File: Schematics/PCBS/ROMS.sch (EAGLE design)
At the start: 12 parts, among them IC1 ATMEGA328P-AU, M1 WIRELESS-NRF24L01-PA-EXT, Y1 16MHz

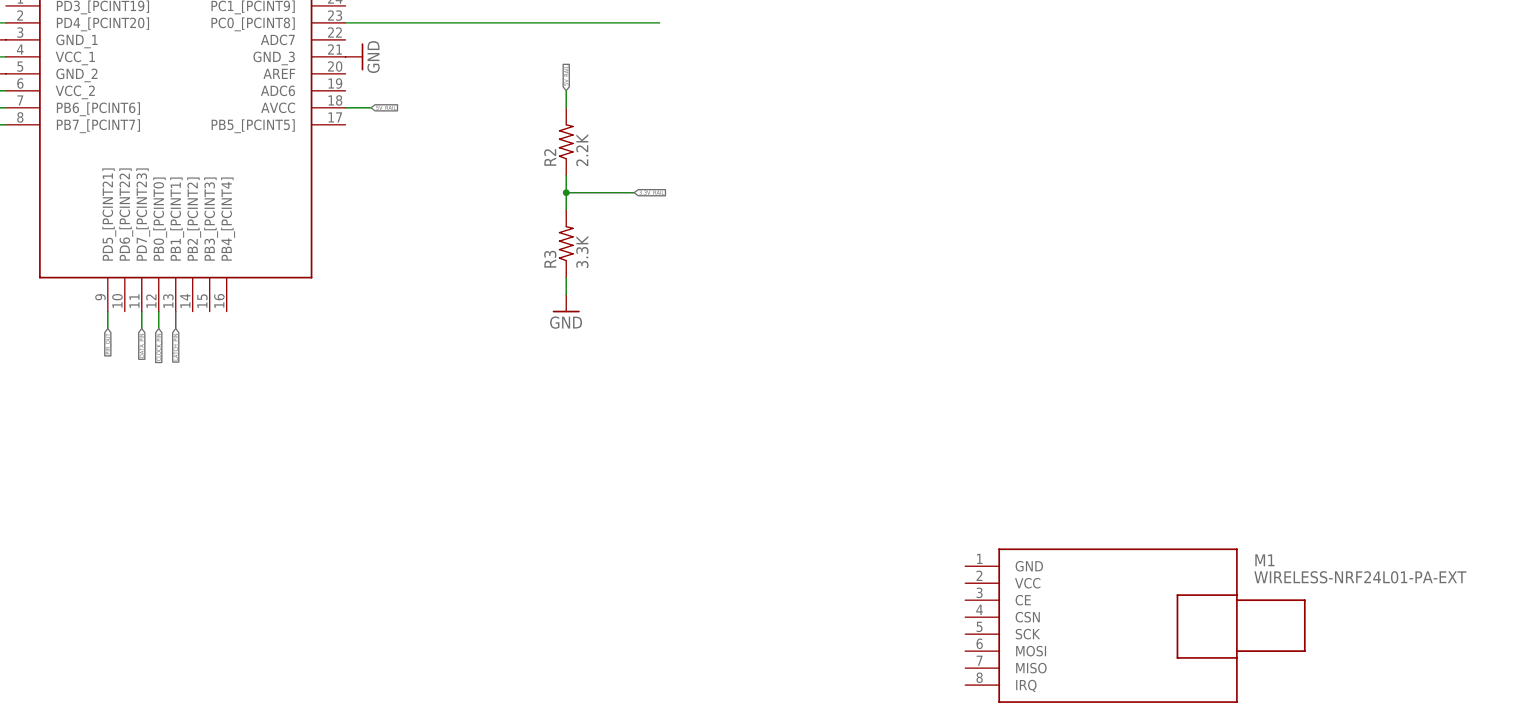
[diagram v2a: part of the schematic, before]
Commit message: connected NRF24 to ATMEGA328p
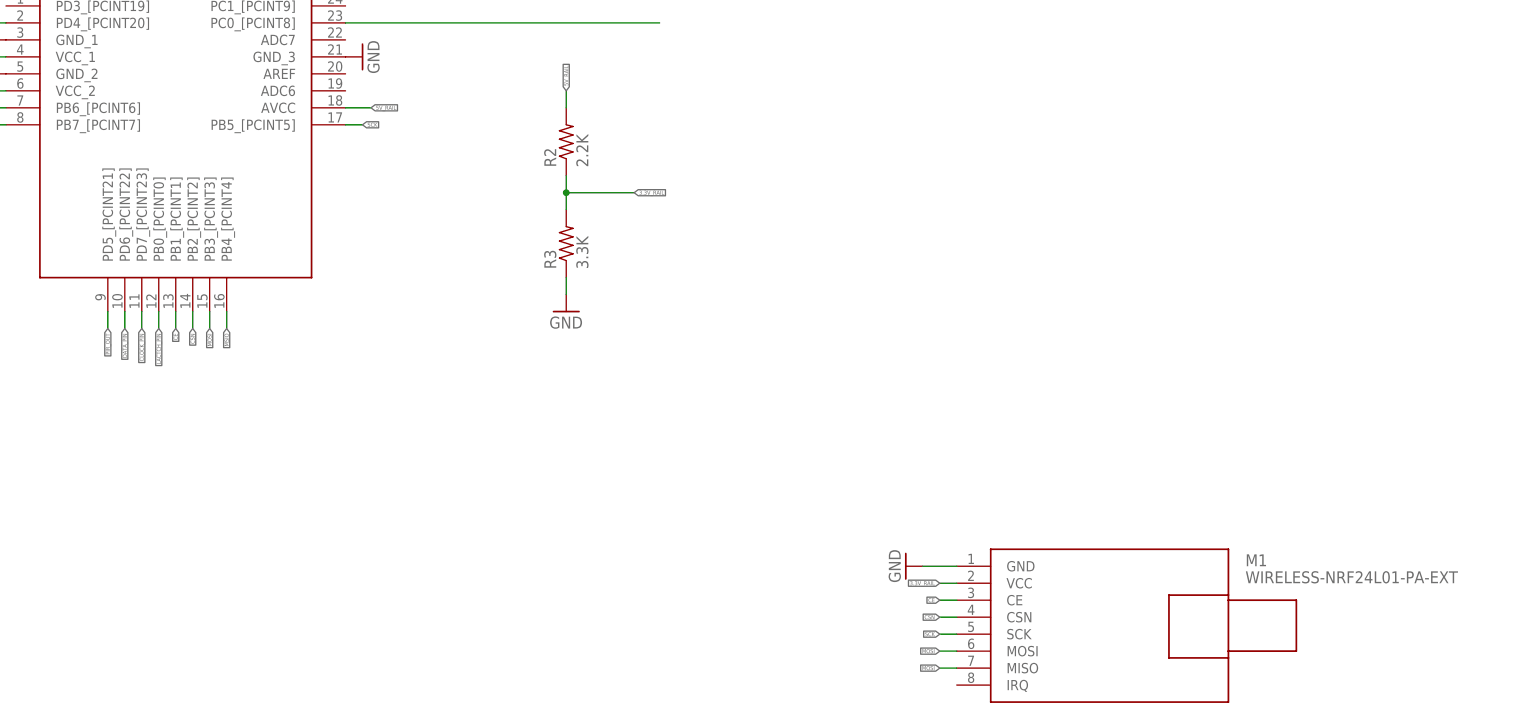
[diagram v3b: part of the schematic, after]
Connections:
- new net CE: IC1.PB1_[PCINT1], M1.CE
- new net CSN: IC1.PB2_[PCINT2], M1.CSN
- new net LACTCH_PIN: IC1.PB0_[PCINT0]
- new net MOSI: IC1.PB3_[PCINT3], M1.MISO, M1.MOSI
- new net MSIO: IC1.PB4_[PCINT4]
- new net SCK: IC1.PB5_[PCINT5], M1.SCK
- net 3.3V_RAIL: now also M1.VCC
- net CLOCK_PIN: now also IC1.PD7_[PCINT23]; no longer IC1.PB0_[PCINT0]
- net DATA_PIN: now also IC1.PD6_[PCINT22]; no longer IC1.PD7_[PCINT23]
- net GND: now also M1.GND
- net LATCH_PIN: no longer IC1.PB1_[PCINT1]
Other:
- moved on the sheet: M1
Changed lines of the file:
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@@
 <part name="R2" library="adafruit" library_urn="urn:adsk.eagle:library:420" deviceset="FLIPFLOP-RES" device="" package3d_urn="urn:adsk.eagle:package:6240726/1" value="2.2K"/>
 <part name="R3" library="adafruit" library_urn="urn:adsk.eagle:library:420" deviceset="FLIPFLOP-RES" device="" package3d_urn="urn:adsk.eagle:package:6240726/1" value="3.3K"/>
+<part name="GND11" library="supply1" library_urn="urn:adsk.eagle:library:371" deviceset="GND" device=""/>
 </parts>
 <sheets>
@@
 <attribute name="VALUE" x="69.85" y="101.6" size="1.778" layer="96" rot="R90"/>
 </instance>
-<instance part="M1" gate="G$1" x="217.17" y="-45.72" smashed="yes">
-<attribute name="NAME" x="237.49" y="-35.56" size="1.778" layer="95"/>
-<attribute name="VALUE" x="237.49" y="-38.1" size="1.778" layer="96"/>
+<instance part="M1" gate="G$1" x="215.9" y="-45.72" smashed="yes">
+<attribute name="NAME" x="236.22" y="-35.56" size="1.778" layer="95"/>
+<attribute name="VALUE" x="236.22" y="-38.1" size="1.778" layer="96"/>
 </instance>
 <instance part="GND7" gate="1" x="134.62" y="2.54" smashed="yes">
@@
 <attribute name="NAME" x="133.1214" y="8.89" size="1.778" layer="95" rot="R90"/>
 <attribute name="VALUE" x="137.922" y="8.89" size="1.778" layer="96" rot="R90"/>
+</instance>
+<instance part="GND11" gate="1" x="185.42" y="-35.56" smashed="yes" rot="R270">
+<attribute name="VALUE" x="182.88" y="-33.02" size="1.778" layer="96" rot="R270"/>
 </instance>
 </instances>
@@
 <pinref part="GND10" gate="1" pin="GND"/>
 </segment>
+<segment>
+<pinref part="M1" gate="G$1" pin="GND"/>
+<wire x1="193.04" y1="-35.56" x2="187.96" y2="-35.56" width="0.1524" layer="91"/>
+<pinref part="GND11" gate="1" pin="GND"/>
+</segment>
 </net>
 <net name="N$3" class="0">
@@
 <label x="-7.62" y="154.94" size="0.762" layer="95" xref="yes"/>
 </segment>
-<segment>
-<pinref part="IC1" gate="G$1" pin="PB1_[PCINT1]"/>
-<wire x1="76.2" y1="2.54" x2="76.2" y2="0" width="0.1524" layer="91"/>
-<label x="76.2" y="0" size="0.6096" layer="95" rot="R270" xref="yes"/>
-</segment>
 </net>
 <net name="CLOCK_PIN" class="0">
@@
 </segment>
 <segment>
-<pinref part="IC1" gate="G$1" pin="PB0_[PCINT0]"/>
-<wire x1="73.66" y1="2.54" x2="73.66" y2="0" width="0.1524" layer="91"/>
-<label x="73.66" y="0" size="0.6096" layer="95" rot="R270" xref="yes"/>
+<pinref part="IC1" gate="G$1" pin="PD7_[PCINT23]"/>
+<wire x1="71.12" y1="2.54" x2="71.12" y2="0" width="0.1524" layer="91"/>
+<label x="71.12" y="0" size="0.6096" layer="95" rot="R270" xref="yes"/>
 </segment>
 </net>
@@
 </segment>
 <segment>
-<pinref part="IC1" gate="G$1" pin="PD7_[PCINT23]"/>
-<wire x1="71.12" y1="2.54" x2="71.12" y2="0" width="0.1524" layer="91"/>
-<label x="71.12" y="0" size="0.6096" layer="95" rot="R270" xref="yes"/>
+<pinref part="IC1" gate="G$1" pin="PD6_[PCINT22]"/>
+<wire x1="68.58" y1="2.54" x2="68.58" y2="0" width="0.1524" layer="91"/>
+<label x="68.58" y="0" size="0.6096" layer="95" rot="R270" xref="yes"/>
 </segment>
 </net>
@@
 <junction x="134.62" y="20.32"/>
 </segment>
-</net>
+<segment>
+<pinref part="M1" gate="G$1" pin="VCC"/>
+<wire x1="193.04" y1="-38.1" x2="190.5" y2="-38.1" width="0.1524" layer="91"/>
+<label x="190.5" y="-38.1" size="0.6096" layer="95" rot="R180" xref="yes"/>
+</segment>
+</net>
+<net name="MOSI" class="0">
+<segment>
+<pinref part="IC1" gate="G$1" pin="PB3_[PCINT3]"/>
+<wire x1="81.28" y1="2.54" x2="81.28" y2="0" width="0.1524" layer="91"/>
+<label x="81.28" y="0" size="0.6096" layer="95" rot="R270" xref="yes"/>
+</segment>
+<segment>
+<pinref part="M1" gate="G$1" pin="MOSI"/>
+<wire x1="193.04" y1="-48.26" x2="190.5" y2="-48.26" width="0.1524" layer="91"/>
+<label x="190.5" y="-48.26" size="0.6096" layer="95" rot="R180" xref="yes"/>
+</segment>
+<segment>
+<pinref part="M1" gate="G$1" pin="MISO"/>
+<wire x1="193.04" y1="-50.8" x2="190.5" y2="-50.8" width="0.1524" layer="91"/>
+<label x="190.5" y="-50.8" size="0.6096" layer="95" rot="R180" xref="yes"/>
+</segment>
+</net>
+<net name="MSIO" class="0">
+<segment>
+<pinref part="IC1" gate="G$1" pin="PB4_[PCINT4]"/>
+<wire x1="83.82" y1="2.54" x2="83.82" y2="0" width="0.1524" layer="91"/>
+<label x="83.82" y="0" size="0.6096" layer="95" rot="R270" xref="yes"/>
+</segment>
+</net>
+<net name="CE" class="0">
+<segment>
+<pinref part="M1" gate="G$1" pin="CE"/>
+<wire x1="193.04" y1="-40.64" x2="190.5" y2="-40.64" width="0.1524" layer="91"/>
+<label x="190.5" y="-40.64" size="0.6096" layer="95" rot="R180" xref="yes"/>
+</segment>
+<segment>
+<pinref part="IC1" gate="G$1" pin="PB1_[PCINT1]"/>
+<wire x1="76.2" y1="2.54" x2="76.2" y2="0" width="0.1524" layer="91"/>
+<label x="76.2" y="0" size="0.6096" layer="95" rot="R270" xref="yes"/>
+</segment>
+</net>
+<net name="CSN" class="0">
+<segment>
+<pinref part="M1" gate="G$1" pin="CSN"/>
+<wire x1="193.04" y1="-43.18" x2="190.5" y2="-43.18" width="0.1524" layer="91"/>
+<label x="190.5" y="-43.18" size="0.6096" layer="95" rot="R180" xref="yes"/>
+</segment>
+<segment>
+<pinref part="IC1" gate="G$1" pin="PB2_[PCINT2]"/>
+<wire x1="78.74" y1="2.54" x2="78.74" y2="0" width="0.1524" layer="91"/>
+<label x="78.74" y="0" size="0.6096" layer="95" rot="R270" xref="yes"/>
+</segment>
+</net>
+<net name="SCK" class="0">
+<segment>
+<pinref part="IC1" gate="G$1" pin="PB5_[PCINT5]"/>
+<wire x1="101.6" y1="30.48" x2="104.14" y2="30.48" width="0.1524" layer="91"/>
+<label x="104.14" y="30.48" size="0.6096" layer="95" xref="yes"/>
+</segment>
+<segment>
+<pinref part="M1" gate="G$1" pin="SCK"/>
+<wire x1="193.04" y1="-45.72" x2="190.5" y2="-45.72" width="0.1524" layer="91"/>
+<label x="190.5" y="-45.72" size="0.6096" layer="95" rot="R180" xref="yes"/>
+</segment>
+</net>
+<net name="LACTCH_PIN" class="0">
+<segment>
+<pinref part="IC1" gate="G$1" pin="PB0_[PCINT0]"/>
+<wire x1="73.66" y1="2.54" x2="73.66" y2="0" width="0.1524" layer="91"/>
+<label x="73.66" y="0" size="0.6096" layer="95" rot="R270" xref="yes"/>
+</segment>
+</net>

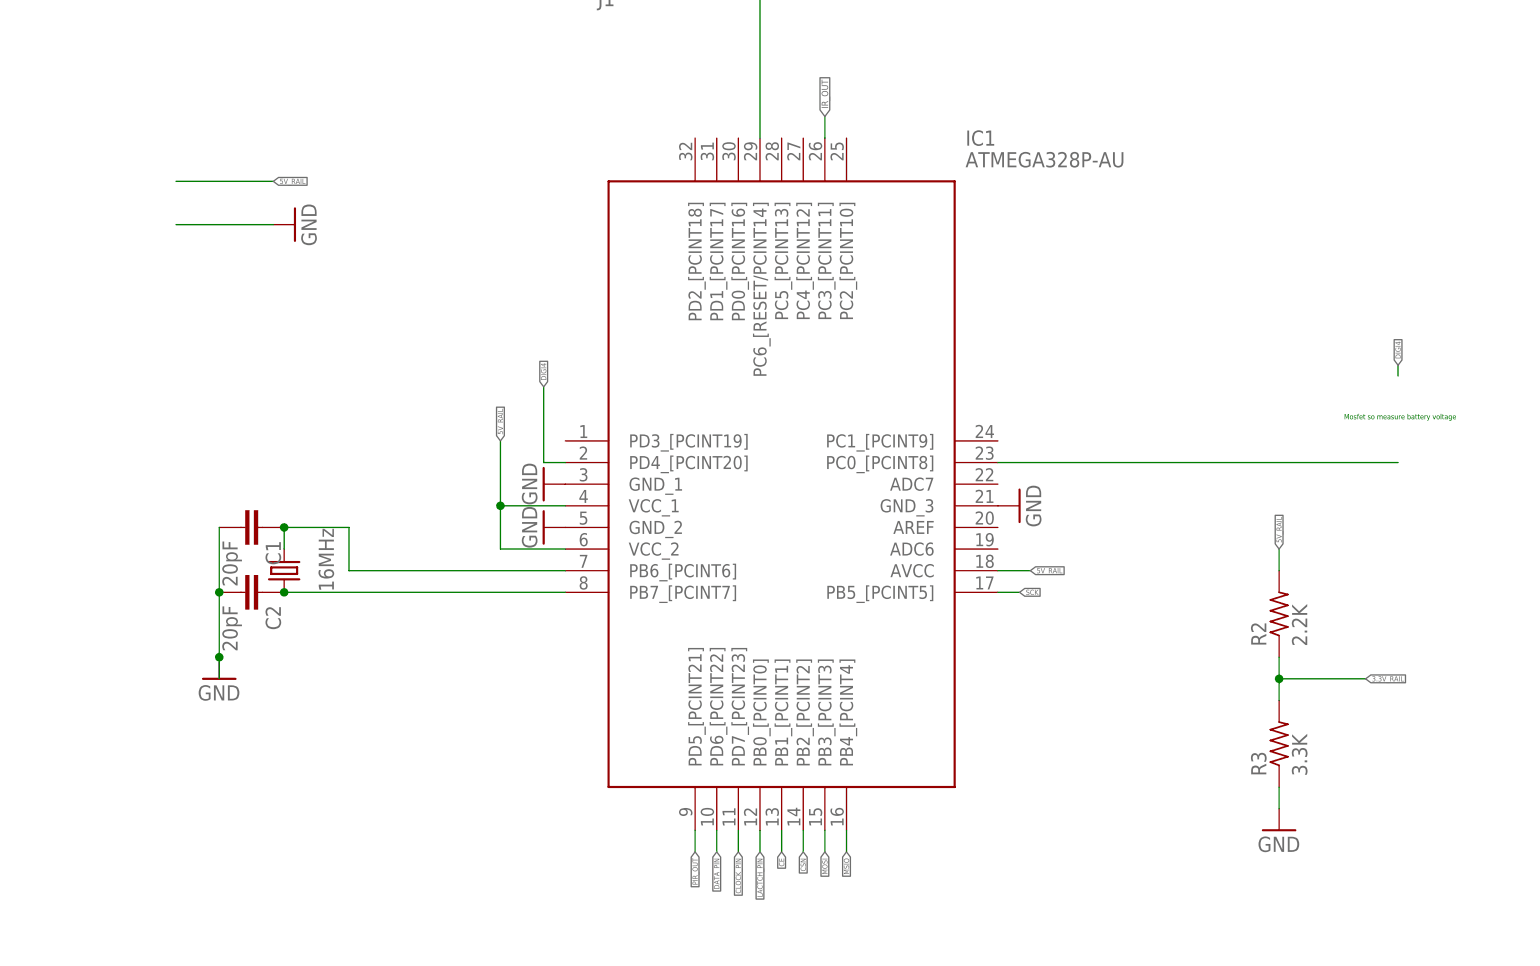
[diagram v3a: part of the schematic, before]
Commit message: added Aluminum Electrolytic Capacitor for stabilizing power
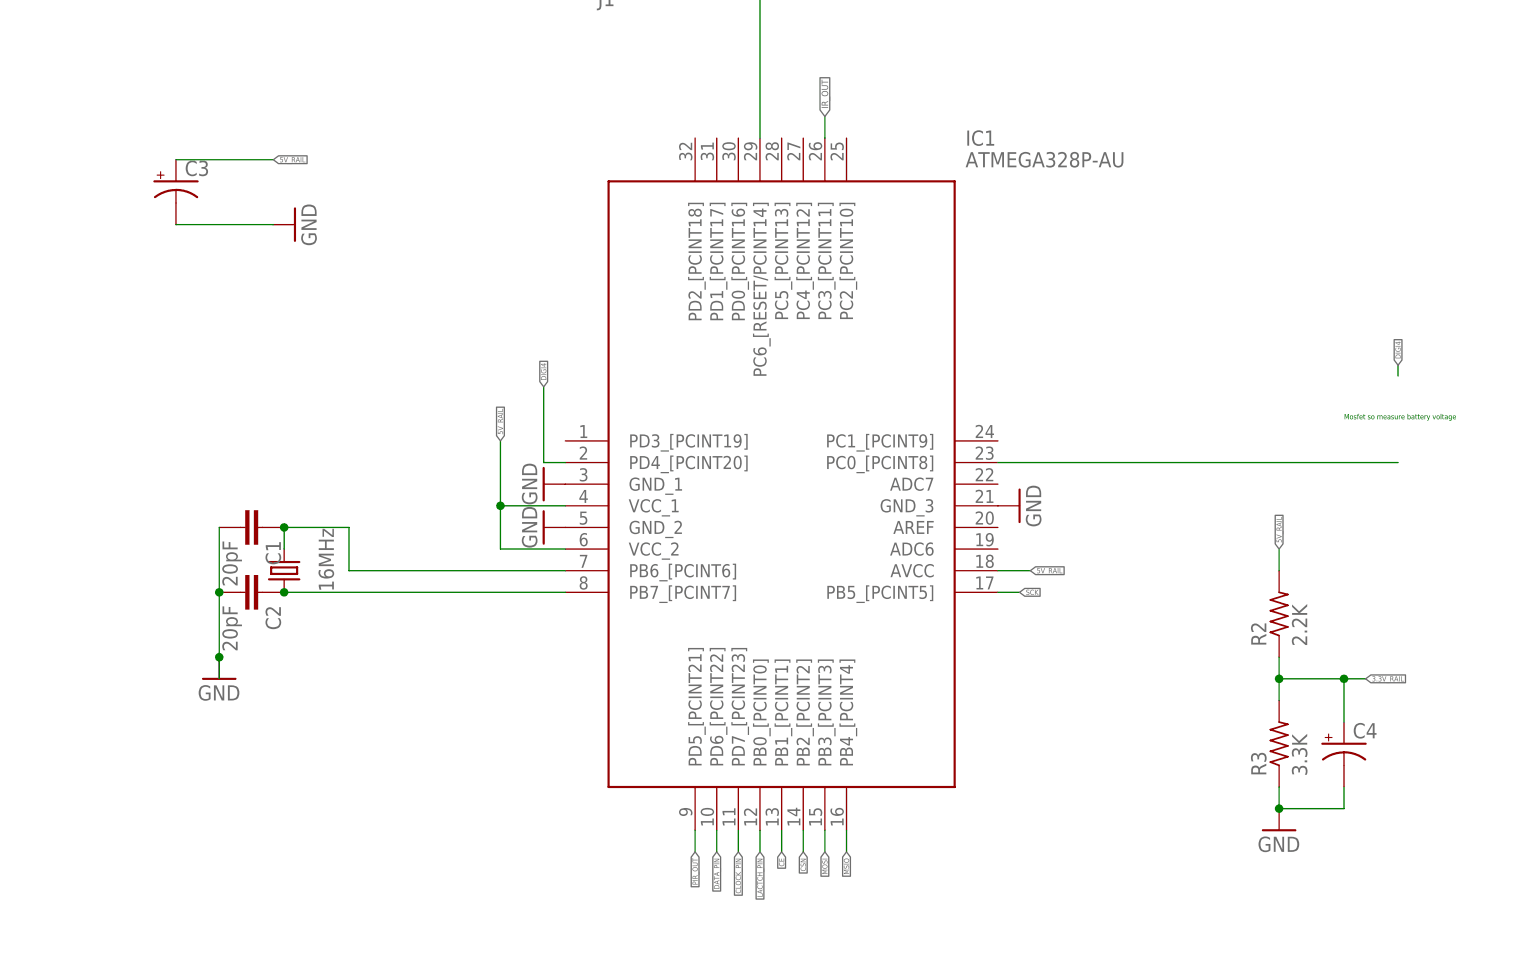
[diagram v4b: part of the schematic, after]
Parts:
- added C3, C4: (no value), adafruit:CPOL-USTT2D5
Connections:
- net 3.3V_RAIL: now also C4.+
- net 5V_RAIL: now also C3.+
- net GND: now also C3.-, C4.-
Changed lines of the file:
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@@
 <part name="R3" library="adafruit" library_urn="urn:adsk.eagle:library:420" deviceset="FLIPFLOP-RES" device="" package3d_urn="urn:adsk.eagle:package:6240726/1" value="3.3K"/>
 <part name="GND11" library="supply1" library_urn="urn:adsk.eagle:library:371" deviceset="GND" device=""/>
+<part name="C3" library="adafruit" library_urn="urn:adsk.eagle:library:420" deviceset="CPOL-US" device="TT2D5" package3d_urn="urn:adsk.eagle:package:6240414/1"/>
+<part name="C4" library="adafruit" library_urn="urn:adsk.eagle:library:420" deviceset="CPOL-US" device="TT2D5" package3d_urn="urn:adsk.eagle:package:6240414/1"/>
 </parts>
 <sheets>
@@
 <attribute name="VALUE" x="182.88" y="-33.02" size="1.778" layer="96" rot="R270"/>
 </instance>
+<instance part="C3" gate="G$1" x="5.08" y="78.74" smashed="yes">
+<attribute name="NAME" x="6.096" y="79.375" size="1.778" layer="95"/>
+<attribute name="VALUE" x="6.096" y="74.549" size="1.778" layer="96"/>
+</instance>
+<instance part="C4" gate="G$1" x="142.24" y="12.7" smashed="yes">
+<attribute name="NAME" x="143.256" y="13.335" size="1.778" layer="95"/>
+<attribute name="VALUE" x="143.256" y="8.509" size="1.778" layer="96"/>
+</instance>
 </instances>
 <busses>
@@
 <wire x1="5.08" y1="73.66" x2="16.51" y2="73.66" width="0.1524" layer="91"/>
 <pinref part="GND5" gate="1" pin="GND"/>
+<pinref part="C3" gate="G$1" pin="-"/>
 </segment>
 <segment>
@@
 </segment>
 <segment>
+<pinref part="R3" gate="G$1" pin="1"/>
 <pinref part="GND7" gate="1" pin="GND"/>
-<pinref part="R3" gate="G$1" pin="1"/>
 <wire x1="134.62" y1="5.08" x2="134.62" y2="7.62" width="0.1524" layer="91"/>
+<pinref part="C4" gate="G$1" pin="-"/>
+<wire x1="142.24" y1="7.62" x2="142.24" y2="5.08" width="0.1524" layer="91"/>
+<wire x1="142.24" y1="5.08" x2="134.62" y2="5.08" width="0.1524" layer="91"/>
+<junction x="134.62" y="5.08"/>
 </segment>
 <segment>
@@
 </segment>
 <segment>
-<wire x1="5.08" y1="78.74" x2="16.51" y2="78.74" width="0.1524" layer="91"/>
-<label x="16.51" y="78.74" size="0.6096" layer="95" xref="yes"/>
+<wire x1="5.08" y1="81.28" x2="16.51" y2="81.28" width="0.1524" layer="91"/>
+<label x="16.51" y="81.28" size="0.6096" layer="95" xref="yes"/>
+<pinref part="C3" gate="G$1" pin="+"/>
 </segment>
 <segment>
@@
 <label x="144.78" y="20.32" size="0.6096" layer="95" xref="yes"/>
 <wire x1="134.62" y1="20.32" x2="134.62" y2="17.78" width="0.1524" layer="91"/>
-<wire x1="134.62" y1="20.32" x2="144.78" y2="20.32" width="0.1524" layer="91"/>
+<wire x1="134.62" y1="20.32" x2="142.24" y2="20.32" width="0.1524" layer="91"/>
 <junction x="134.62" y="20.32"/>
-</segment>
-<segment>
+<pinref part="C4" gate="G$1" pin="+"/>
+<wire x1="142.24" y1="20.32" x2="144.78" y2="20.32" width="0.1524" layer="91"/>
+<wire x1="142.24" y1="20.32" x2="142.24" y2="15.24" width="0.1524" layer="91"/>
+<junction x="142.24" y="20.32"/>
+</segment>
+<segment>
